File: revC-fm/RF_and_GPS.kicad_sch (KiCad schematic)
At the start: 8 parts, among them J8 SMPM-PS-P-HG-ST-EM-1, J9 SMPM-PS-P-HG-ST-EM-1, U24 RFM98PW, U25 RFM9xBreakout, U26 S1216V8

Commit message: working revC
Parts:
- renumbered C86 to C81, R174 to R156, R175 to R157, U24 to U21, U26 to U22, U25 to U23

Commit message: working revC
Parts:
- added Q1: MMBT2907AM3T5G, Package_TO_SOT_SMD:SOT-723, symbol Device:Q_PNP_BEC
- added Q5: BSZ180P03NS3GATMA1, SierraLobo:PG-TSDSON-8_3.3x3.3mm, symbol SierraLobo:BSZ086
- added R195, R65: 100k, Resistor_SMD:R_0603_1608Metric, symbol Device:R_US
- added R23: 1k, Resistor_SMD:R_0603_1608Metric, symbol Device:R_US
- J2: renamed from J8; footprint mainboard-SLI:J-MOLEX-SMPM-073300-003X_no_Back -> SierraLobo:SMPM-073300-003X_no_Back
- J3: renamed from J9; footprint mainboard-SLI:J-MOLEX-SMPM-073300-003X_no_Back -> SierraLobo:SMPM-073300-003X_no_Back
- U20: renamed from U21; footprint mainboard:RFM95PW -> SierraLobo:RFM95PW; symbol mainboard:RFM98PW -> SierraLobo:RFM98PW; Flight RFM98PW -> (none); Manufacturer_Name HopeRF -> (none); Manufacturer_Part_Number RFM98PW -> (none); Proto RFM98PW -> (none)
- U21: renamed from U22; value S1216V8 -> ORION B16; footprint mainboard:S1216_24PIN_PACKAGE -> SierraLobo:S1216_24PIN_PACKAGE; symbol mainboard:S1216V8 -> SierraLobo:S1216V8; DNI DNI -> (none)
- U22: renamed from U23; symbol mainboard:RFM9xBreakout -> SierraLobo:RFM9xBreakout; DNI DNI -> (none); now not fitted
- renumbered C81 to C85, R156 to R188, R157 to R189
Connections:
- net 3.3V: now also Q1.2 (E), Q5.1 (S)
- net GND: now also R195.2
- net GPS_PWR_IN: now also Q5.5 (D)
- net at U21.1 (NC): now also U21.14 (NC), U21.15 (NC), U21.16 (NC), U21.17 (NC), U21.2 (NC), U21.4 (NC), U21.5 (NC), U21.6 (NC), U21.7 (NC), U21.9 (NC)
- new net: Q5.4 (G), R23.1
- new net: Q1.3 (C), R195.1, R23.2
- new net: Q1.1 (B), R65.2
- new net ENAB_GPS: R65.1
- no-connect marks 22 -> 11
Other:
- note added: "GPS Power Switch"
- moved on the sheet: J3, R189

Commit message: routing fm
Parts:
- removed Q1: MMBT2907AM3T5G, Package_TO_SOT_SMD:SOT-723, symbol Device:Q_PNP_BEC
- removed R65: 100k, Resistor_SMD:R_0603_1608Metric, symbol Device:R_US
- added C103: 10uF, Capacitor_SMD:C_0805_2012Metric, symbol Device:C_Small
- added J1: SMPM-PS-P-HG-ST-EM-1, SierraLobo:SMPM-073300-003X_no_Back, symbol mainboard-rescue:Conn_Coaxial-Connector-mainboard-rescue
- added Q42 (x3): ~, Package_TO_SOT_SMD:SOT-323_SC-70, symbol Device:Q_NPN_BEC
- added Q5 (x2): BSZ180P03NS3GATMA1, SierraLobo:PG-TSDSON-8_3.3x3.3mm, symbol SierraLobo:BSZ086
- added R128: 10k, Resistor_SMD:R_0603_1608Metric, symbol Device:R_US
- added R195 (x2), R196 (x3): 100k, Resistor_SMD:R_0603_1608Metric, symbol Device:R_US
- added R23 (x2), R239, R240, R241, R242, R243, R244, R245, R246, R247, R248: 1k, Resistor_SMD:R_0603_1608Metric, symbol Device:R_US
- added U26: RFM98PW, SierraLobo:RFM95PW, symbol SierraLobo:RFM98PW
- added U29: RFM9xBreakout, RF_Module:HOPERF_RFM9XW_SMD, symbol SierraLobo:RFM9xBreakout
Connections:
- net 3.3V: now also R195.1, Q5.1 (S), Q5.1 (S), R195.1, R195.1; no longer C85.2, R188.1, U20.5 (VCC), U20.9 (3.3V), U22.13 (3V3)
- net ENAB_GPS: now also R196.2
- net GND: now also C103.1, J1.2 (Ext), Q42.2 (E), Q42.2 (E), Q42.2 (E), U26.16 (GND), U26.17 (GND), U26.2 (GND), U29.1 (GND), U29.10 (GND), U29.8 (GND); no longer R195.2
- net RF1_CS: now also R243.1; no longer U20.13 (NSS), U22.5 (CS)
- net RF1_IO0: now also R240.1; no longer U20.6 (GPIO_0), U22.14 (DIO0)
- net RF1_IO4: now also R241.2; no longer U20.4 (GPIO_4), U22.12 (BUSY)
- net RF1_RST: now also R239.1; no longer U20.14 (RESET), U22.6 (~{RESET})
- net RX_MCU: now also R247.1; no longer U21.20 (TXD)
- net TX_MCU: now also R248.1; no longer U21.21 (RXD)
- net at R23.2: now also R195.2, Q42.3 (C); no longer R195.1
- new net: R247.2, U21.20 (TXD)
- new net: R248.2, U21.21 (RXD)
- new net: Q42.1 (B), R196.1 (x3)
- new net: Q42.3 (C), R195.2, R23.2 (x2)
- new net: Q5.4 (G), R23.1 (x2)
- new net ENAB_RF1: R196.2
- new net ENAB_RF2: R196.2
- new net MISO_RF2: U26.10 (MISO), U29.2 (MISO)
- new net MOSI_RF2: U26.11 (MOSI), U29.3 (MOSI)
- new net RF1_PWR_IN: C85.2, Q5.5 (D), R188.1, U20.5 (VCC), U20.9 (3.3V), U22.13 (3V3)
- new net RF2_ANT: J1.1 (In), U26.1 (ANT), U29.9 (ANT)
- new net RF2_CS: R128.2, R244.1
- new net RF2_IO0: R245.1
- new net RF2_IO4: R242.2
- new net RF2_PWR_IN: C103.2, Q5.5 (D), R128.1, U26.5 (VCC), U26.9 (3.3V), U29.13 (3V3)
- new net RF2_RST: R246.1
- new net RF_1_CS: R243.2, U20.13 (NSS), U22.5 (CS)
- new net RF_1_IO0: R240.2, U20.6 (GPIO_0), U22.14 (DIO0)
- new net RF_1_IO4: R241.1, U20.4 (GPIO_4), U22.12 (BUSY)
- new net RF_1_RST: R239.2, U20.14 (RESET), U22.6 (~{RESET})
- new net RF_2_CS: R244.2, U26.13 (NSS), U29.5 (CS)
- new net RF_2_IO0: R245.2, U26.6 (GPIO_0), U29.14 (DIO0)
- new net RF_2_IO4: R242.1, U26.4 (GPIO_4), U29.12 (BUSY)
- new net RF_2_RST: R246.2, U26.14 (RESET), U29.6 (~{RESET})
- new net SCK_RF2: U26.12 (SCK), U29.4 (SCK)
- no-connect marks 11 -> 19
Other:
- added sheet Temp Sensor 4 (temp_senkicad_sch.kicad_sch)
- added sheet Temp Sensor 5 (temp_senkicad_sch.kicad_sch)
- note added: "RF1 Power Switch"
- note added: "RF2 Power Switch"
- note added: "Radio #2"
- moved on the sheet: C85, J2, J3, Q5, R188, R189, R195, R23, U20, U21, U22

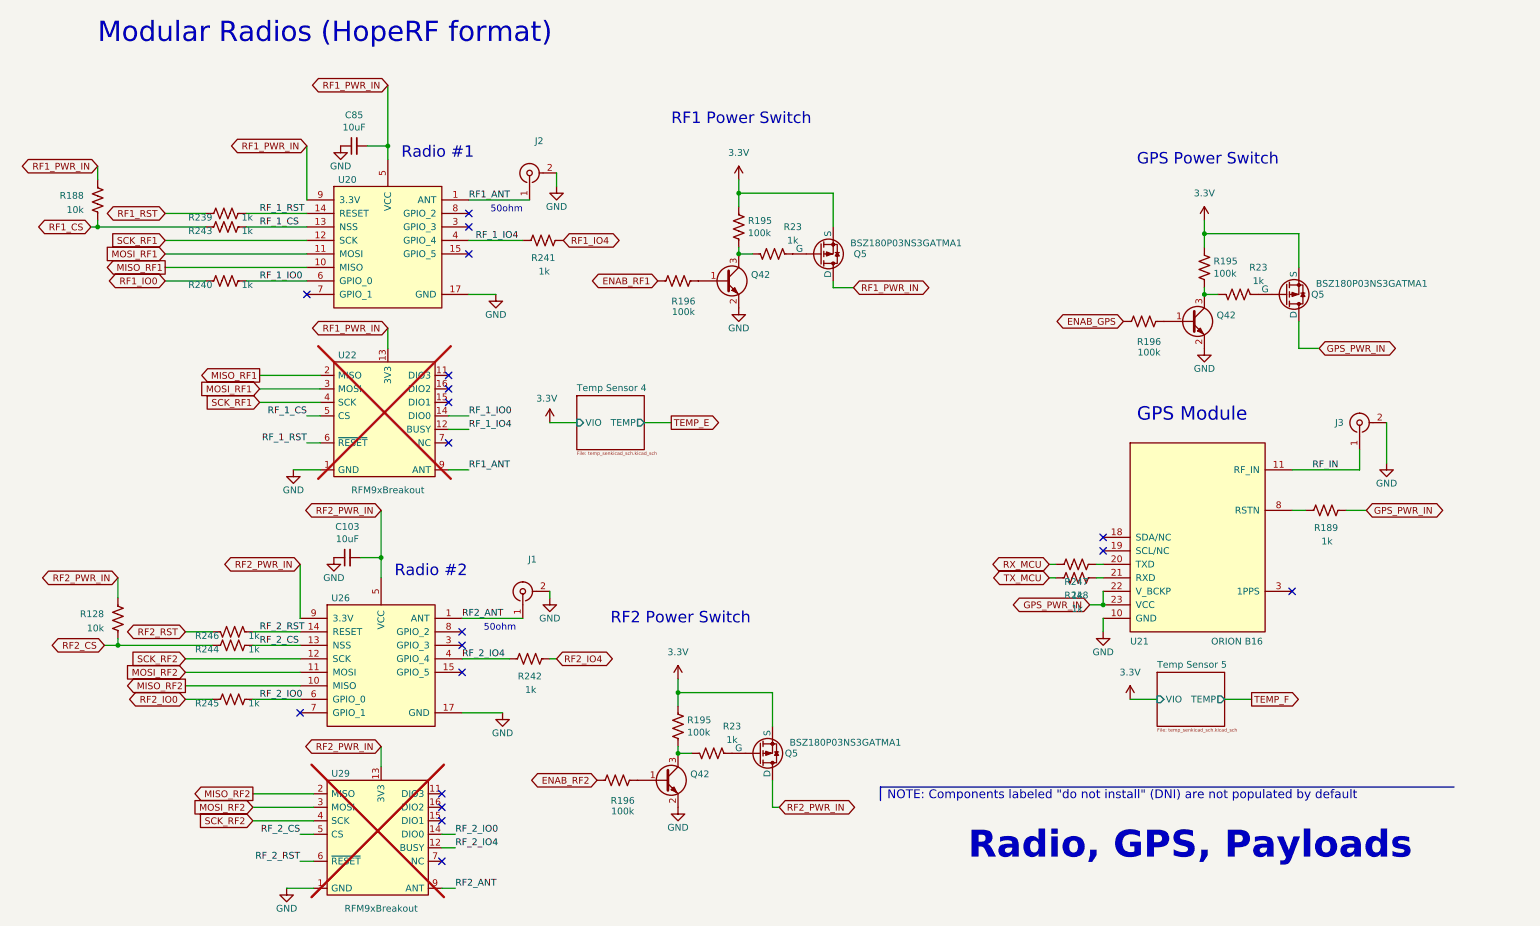
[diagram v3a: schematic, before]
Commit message: updated analog , solar comp, layout
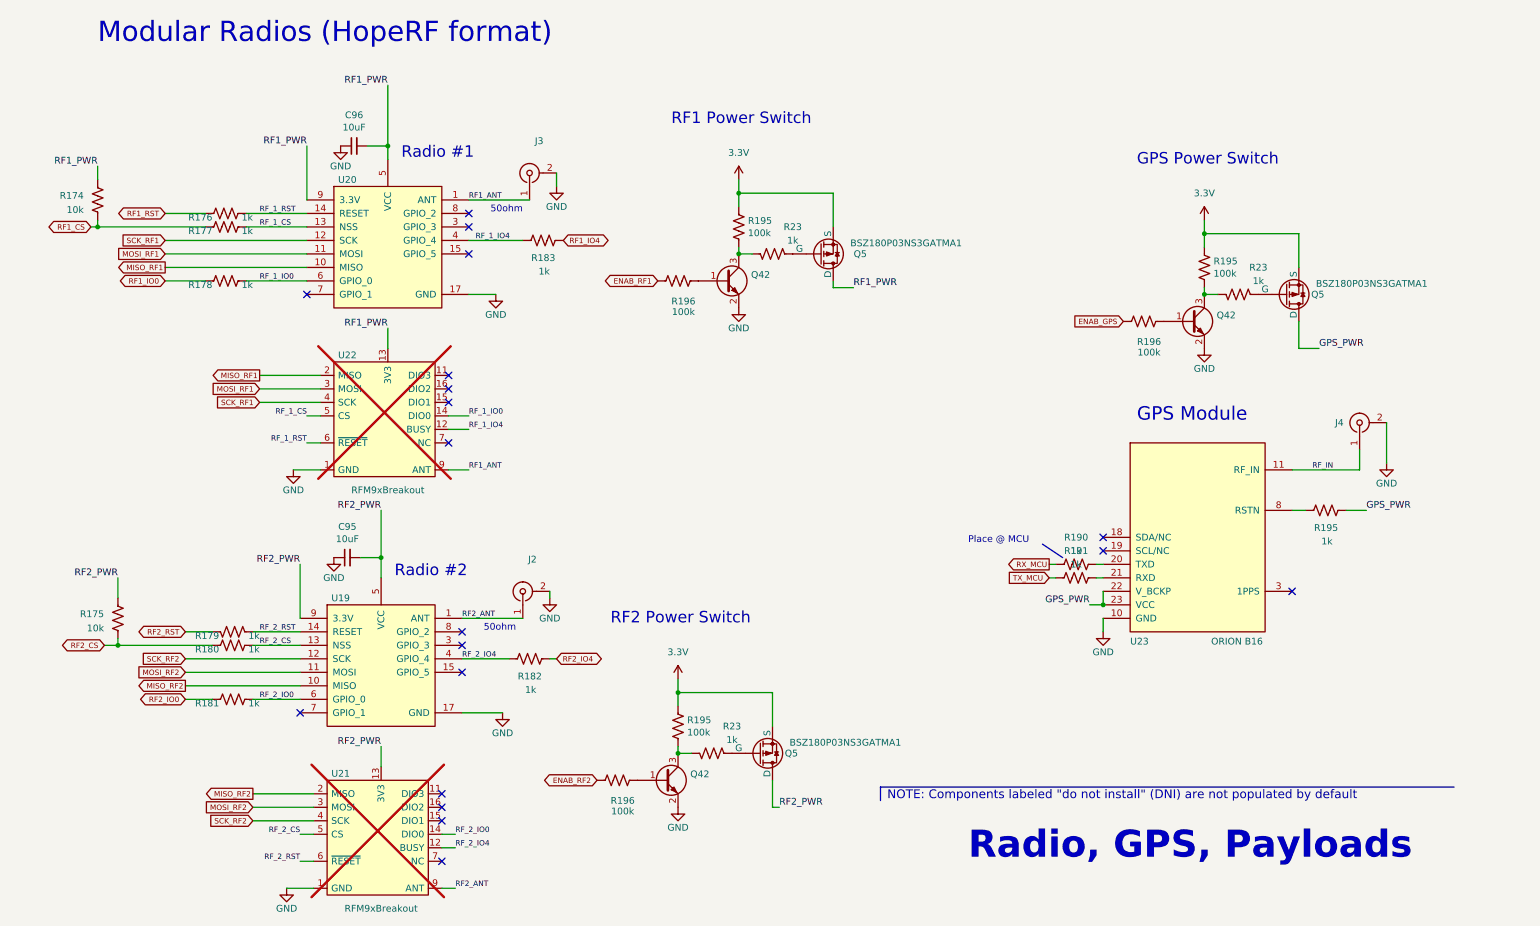
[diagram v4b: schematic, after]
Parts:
- renumbered C103 to C95, C85 to C96, J1 to J2, J2 to J3, J3 to J4, R188 to R174, R128 to R175, R239 to R176, R243 to R177, R240 to R178, R246 to R179, R244 to R180, R245 to R181, R242 to R182, R241 to R183, R247 to R190, R248 to R191, R189 to R195, U26 to U19, U29 to U21, U21 to U23
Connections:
- net GPS_PWR_IN renamed GPS_PWR
- net RF1_PWR_IN renamed RF1_PWR
- net RF2_PWR_IN renamed RF2_PWR
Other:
- removed sheet Temp Sensor 4
- removed sheet Temp Sensor 5
- note added: "Place @ MCU"

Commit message: routing
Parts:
- renumbered C96 to C100, C95 to C101, J3 to J2, J4 to J3, J2 to J4, R174 to R161, R176 to R162, R177 to R163, R183 to R165, R178 to R168, R195 to R172, R190 to R173, R191 to R174, R179 to R176, R180 to R177, R182 to R178, R181 to R179, U20 to U21, U19 to U24, U21 to U25

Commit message: fm layout
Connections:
- now unconnected: U23.1 (NC), U23.14 (NC), U23.15 (NC), U23.16 (NC), U23.17 (NC), U23.2 (NC), U23.4 (NC), U23.5 (NC), U23.6 (NC), U23.7 (NC), U23.9 (NC)
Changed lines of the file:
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@@
   (no_connect (at 95.25 90.17))
   (no_connect (at 99.06 62.23))
-  (no_connect (at 254 125.73))
+  (no_connect (at 254 115.57))
   (no_connect (at 93.98 176.53))
   (no_connect (at 99.06 57.15))
@@
     (stroke (width 0) (type default))
   )
-  (wire (pts (xy 209.55 120.65) (xy 208.28 120.65))
+  (wire (pts (xy 209.55 120.65) (xy 204.47 120.65))
     (stroke (width 0) (type default))
   )
@@
     (stroke (width 0) (type default))
   )
-  (wire (pts (xy 218.44 128.27) (xy 215.9 128.27))
+  (wire (pts (xy 218.44 128.27) (xy 204.47 128.27))
     (stroke (width 0) (type default))
   )
@@
     (stroke (width 0) (type default))
   )
-  (wire (pts (xy 209.55 123.19) (xy 208.28 123.19))
+  (wire (pts (xy 209.55 123.19) (xy 204.47 123.19))
     (stroke (width 0) (type default))
   )
@@
     (effects (font (size 1.016 1.016)) (justify left bottom))
   )
-  (label "GPS_PWR" (at 215.9 128.27 180) (fields_autoplaced)
+  (label "GPS_PWR" (at 204.47 128.27 180) (fields_autoplaced)
     (effects (font (size 1.016 1.016)) (justify right bottom))
   )
@@
     )
   )
-  (global_label "TX_MCU" (shape input) (at 208.28 123.19 180) (fields_autoplaced)
-    (effects (font (size 1.016 1.016)) (justify right))
-    (property "Intersheetrefs" "${INTERSHEET_REFS}" (at 200.7214 123.19 0)
+  (global_label "TX_MCU" (shape input) (at 204.47 123.19 180) (fields_autoplaced)
+    (effects (font (size 1.016 1.016)) (justify right))
+    (property "Intersheetrefs" "${INTERSHEET_REFS}" (at 196.9114 123.19 0)
       (effects (font (size 1.016 1.016)) (justify right) hide)
     )
@@
     )
   )
-  (global_label "RX_MCU" (shape output) (at 208.28 120.65 180) (fields_autoplaced)
-    (effects (font (size 1.016 1.016)) (justify right))
-    (property "Intersheetrefs" "${INTERSHEET_REFS}" (at 200.4795 120.65 0)
+  (global_label "RX_MCU" (shape output) (at 204.47 120.65 180) (fields_autoplaced)
+    (effects (font (size 1.016 1.016)) (justify right))
+    (property "Intersheetrefs" "${INTERSHEET_REFS}" (at 196.6695 120.65 0)
       (effects (font (size 1.016 1.016)) (justify right) hide)
     )
@@
   )
   (symbol (lib_id "Device:R_US") (at 213.36 120.65 90) (unit 1)
-    (in_bom yes) (on_board yes) (dnp no) (fields_autoplaced)
-    (property "Reference" "R173" (at 213.36 115.57 90)
-      (effects (font (size 1.27 1.27)))
-    )
-    (property "Value" "1k" (at 213.36 118.11 90)
+    (in_bom yes) (on_board yes) (dnp no)
+    (property "Reference" "R173" (at 208.28 119.38 90)
+      (effects (font (size 1.27 1.27)))
+    )
+    (property "Value" "1k" (at 217.17 119.38 90)
       (effects (font (size 1.27 1.27)))
     )
@@
   )
   (symbol (lib_id "Device:R_US") (at 213.36 123.19 90) (unit 1)
-    (in_bom yes) (on_board yes) (dnp no) (fields_autoplaced)
-    (property "Reference" "R174" (at 213.36 118.11 90)
-      (effects (font (size 1.27 1.27)))
-    )
-    (property "Value" "1k" (at 213.36 120.65 90)
-      (effects (font (size 1.27 1.27)))
-    )
+    (in_bom yes) (on_board yes) (dnp no)
+    (property "Reference" "R174" (at 208.28 121.92 90)
+      (effects (font (size 1.27 1.27)))
+    )
+    (property "Value" "1k" (at 217.17 121.92 90)
+      (effects (font (size 1.27 1.27)))
+    )

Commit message: changed RF connector to TH
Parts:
- J2, J3: value SMPM-PS-P-HG-ST-EM-1 -> SMPM-PS-P-HG-ST-TH-1; footprint SierraLobo:SMPM-073300-003X_no_Back -> SierraLobo:SAMTEC_SMPM-PS-P-HG-ST-TH-1; Mfr. Part No (none) -> SMPM-PS-P-HG-ST-TH-1
- J4: value SMPM-PS-P-HG-ST-EM-1 -> SMPM-PS-P-HG-ST-TH-1; footprint SierraLobo:SMPM-073300-003X_no_Back -> SierraLobo:SAMTEC_SMPM-PS-P-HG-ST-TH-1; Mfr. Part No (none) -> SMPM-PS-P-HG-ST-TH-1; now not fitted
- Q42, Q5, R195, R196: now not fitted
- R171: renamed from R175; now not fitted
- R172: renamed from R176; now not fitted
- R173: renamed from R177; now not fitted
- R174: renamed from R178; now not fitted
- R175: renamed from R179; now not fitted
- U22: renamed from U24; now not fitted
- renumbered C100 to C90, C101 to C91, R161 to R157, R162 to R158, R163 to R159, R165 to R161, R168 to R164, R172 to R168, R173 to R169, R174 to R170, U21 to U19, U22 to U20, U23 to U21, U25 to U23

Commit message: working revC review changes
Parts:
- added Q5 (x3): BSZ180P03NS3GATMA1, SierraLobo:PG-TSDSON-8_3.3x3.3mm, symbol SierraLobo:BSZ086
- added R23 (x3): 1k, Resistor_SMD:R_0603_1608Metric, symbol Device:R_US
- C92: renamed from C91; now not fitted
- R23: now not fitted
- renumbered C90 to C91, R157 to R173, R158 to R174, R159 to R177, R161 to R178, R164 to R181, R168 to R182, R169 to R183, R170 to R184, R171 to R185, R172 to R186, R173 to R187, R174 to R188, R175 to R189, U19 to U20, U20 to U21, U21 to U22, U22 to U23, U23 to U24
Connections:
- net 3.3V: now also Q5.1 (S), Q5.1 (S), Q5.1 (S)
- net GPS_PWR: now also Q5.5 (D)
- net RF1_PWR: now also Q5.5 (D)
- net RF2_PWR: now also Q5.5 (D)
- net at Q42.3 (C), R195.2, R23.2: now also R23.2 (x3)
- new net: Q5.4 (G), R23.1 (x3)
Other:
- moved on the sheet: Q42, Q5, R195, R196, R23
